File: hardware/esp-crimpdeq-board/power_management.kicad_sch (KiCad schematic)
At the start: 0 parts

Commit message: Added power management
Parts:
- added C15, C16: 4.7uF 16V, Capacitor_SMD:C_0603_1608Metric, symbol Device:C_Small
- added C22, C24: 0.1uF 10V, Capacitor_SMD:C_0402_1005Metric, symbol Device:C_Small
- added C23, C25: 1uF 16V, Capacitor_SMD:C_0402_1005Metric, symbol Device:C_Small
- added C28, C5, C7: 10uF 16V, Capacitor_SMD:C_0805_2012Metric, symbol Device:C_Small
- added C6: 22pF 50V, Capacitor_SMD:C_0603_1608Metric, symbol Device:C_Small
- added D3: LED, LED_SMD:LED_0603_1608Metric, symbol Device:LED
- added D4, D6: B5819W, Diode_SMD:D_SOD-123, symbol Device:D_Schottky
- added D5, D7, D8: LESD5D5.0CT1G, Diode_SMD:D_SOD-523, symbol Device:D_TVS
- added J1: USB4105-GF-A, PCM_GCT:GCT_USB4105-GF-A, symbol PCM_GCT:USB4105-GF-A
- added L1: SPH4018H2R2MT (2.2uH 2.2A), Inductor_SMD:L_Bourns-SRN4018, symbol Device:L_Small
- added Q1: DMG3415U, Package_TO_SOT_SMD:SOT-23, symbol Transistor_FET:DMG2301L
- added R1, R20, R23, R9: 10kR 1%, Resistor_SMD:R_0402_1005Metric, symbol Device:R_Small_US
- added R14: 1kR 1%, Resistor_SMD:R_0402_1005Metric, symbol Device:R_Small_US
- added R15, R2: 100kR 1%, Resistor_SMD:R_0402_1005Metric, symbol Device:R_Small_US
- added R3: 22k1R 1%, Resistor_SMD:R_0402_1005Metric, symbol Device:R_Small_US
- added R4, R6: 5k1R 1%, Resistor_SMD:R_0402_1005Metric, symbol Device:R_Small_US
- added R5: 0R 1%, Resistor_SMD:R_0402_1005Metric, symbol Device:R_Small_US
- added S1: 450404015514, PCM_Wurth_Elektronik:450404015514, symbol PCM_Wurth_Elektronik:450404015514
- added U3: REF35330QDBVR, Package_TO_SOT_SMD:SOT-23-6, symbol Reference_Voltage:REF35330QDBVR
- added U4: MCP1640Bx-xMC, Package_DFN_QFN:DFN-8-1EP_3x2mm_P0.5mm_EP1.75x1.45mm, symbol Regulator_Switching:MCP1640Bx-xMC
- added U6: MCP73831T-2ACI/OT, Package_TO_SOT_SMD:SOT-23-5, symbol Battery_Management:MCP73831-2-OT
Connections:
- new net: C6.2, R2.2, R3.1
- new net: R1.2, S1.3
- new net: J1.B5 (CC2), R4.1
- new net: J1.A5 (CC1), R6.1
- new net: D6.2 (A), D7.1 (A1), J1.A4_B9 (VBUS), J1.B4_A9 (VBUS)
- new net: R9.2, U6.5 (PROG)
- new net: D3.1 (K), R14.2
- new net: C28.1, U3.5 (NR)
- new net: U4.2 (GND), U4.3 (GND), U4.9 (GND)
- new net: U4.6 (V_{OUT}), U4.7 (V_{OUT})
- new net: R23.1, U3.3 (EN)
- new net: J1.S1 (SHELL_GND), J1.S2 (SHELL_GND), J1.S3 (SHELL_GND), J1.S4 (SHELL_GND), R5.1
- new net +3V3: C6.1, C7.1, L1.2, R2.1, R20.2, R23.2
- new net +5V: C22.1, C23.1, C5.1, D4.1 (K), Q1.2 (S), R1.1, U3.4 (VIN)
- new net +BATT_SYS: C16.1, Q1.3 (D), U6.3 (V_{BAT})
- new net Buck_Coil: L1.1
- new net CHARGING: R14.1, R20.1, U6.1 (STAT)
- new net ENABLE: S1.2
- new net GND: C15.1, C16.2, C22.2, C23.2, C24.2, C25.2, C28.2, C5.2, C7.2, D5.2 (A2), D7.2 (A2), D8.2 (A2), J1.A1_B12 (GND), J1.B1_A12 (GND), R15.2, R3.2, R4.2, R5.2, R6.2, R9.1, S1.1, U3.1 (GND), U3.2 (GND), U6.2 (V_{SS})
- new net USB_D+: D8.1 (A1), J1.A6 (DP1), J1.B6 (DP2)
- new net USB_D-: D5.1 (A1), J1.A7 (DN1), J1.B7 (DN2)
- new net VBUS: C15.2, D3.2 (A), D4.2 (A), D6.1 (K), Q1.1 (G), R15.1, U6.4 (V_{DD})
- new net VREF3V3: C24.1, C25.1, U3.6 (VREF)
- no-connect marks 0 -> 2
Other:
- note added: "DC/DC Buck Converter 3V3 Rails"
- note added: "Li-Ion Charge Management Controller"
- note added: "REF. VOLTAGE"
- note added: "Red LED 060 Charging"
- note added: "SIMPLE ON/OFF"
- note added: "USB & Battery Switch"
- note added: "USB Type-C Connector"

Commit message: Pending
Pending
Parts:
- removed U4: MCP1640Bx-xMC, Package_DFN_QFN:DFN-8-1EP_3x2mm_P0.5mm_EP1.75x1.45mm, symbol Regulator_Switching:MCP1640Bx-xMC
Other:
- moved on the sheet: C15, C16, C22, C23, C24, C25, C28, D3, D4, D5, D6, D7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

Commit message: Added secns SY8088 to produce 5 V for fast adc
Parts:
- added C32, C34: 10uF 16V, Capacitor_SMD:C_0805_2012Metric, symbol Device:C_Small
- added C33: 22pF 50V, Capacitor_SMD:C_0603_1608Metric, symbol Device:C_Small
- added L2: SPH4018H2R2MT (2.2uH 2.2A), Inductor_SMD:L_Bourns-SRN4018, symbol Device:L_Small
- added R10: 162kR 1%, Resistor_SMD:R_0402_1005Metric, symbol Device:R_Small_US
- added R13: 22k1R 1%, Resistor_SMD:R_0402_1005Metric, symbol Device:R_Small_US
- added U4, U5: SY8088, Package_TO_SOT_SMD:SOT-23-5, symbol PCM_Silergy:SY8088
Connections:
- net +5V: now also C33.1, C34.1, L2.2, R10.1; no longer C5.1, D4.1 (K), Q1.2 (S), R1.1
- net Buck_Coil: now also L2.1, U4.3 (LX), U5.3 (LX)
- net ENABLE: now also U4.1 (EN), U5.1 (EN)
- net GND: now also C32.2, C34.2, R13.2, U4.2 (GND), U5.2 (GND)
- net at C6.2, R2.2, R3.1: now also U4.5 (FB)
- new net: C33.2, R10.2, R13.1, U5.5 (FB)
- new net VSYS: C32.1, C5.1, D4.1 (K), Q1.2 (S), R1.1, U4.4 (IN), U5.4 (IN)
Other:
- note added: "DC/DC Buck Converter 5V0 Rails"
- moved on the sheet: C5, C6, C7, L1, R2, R3

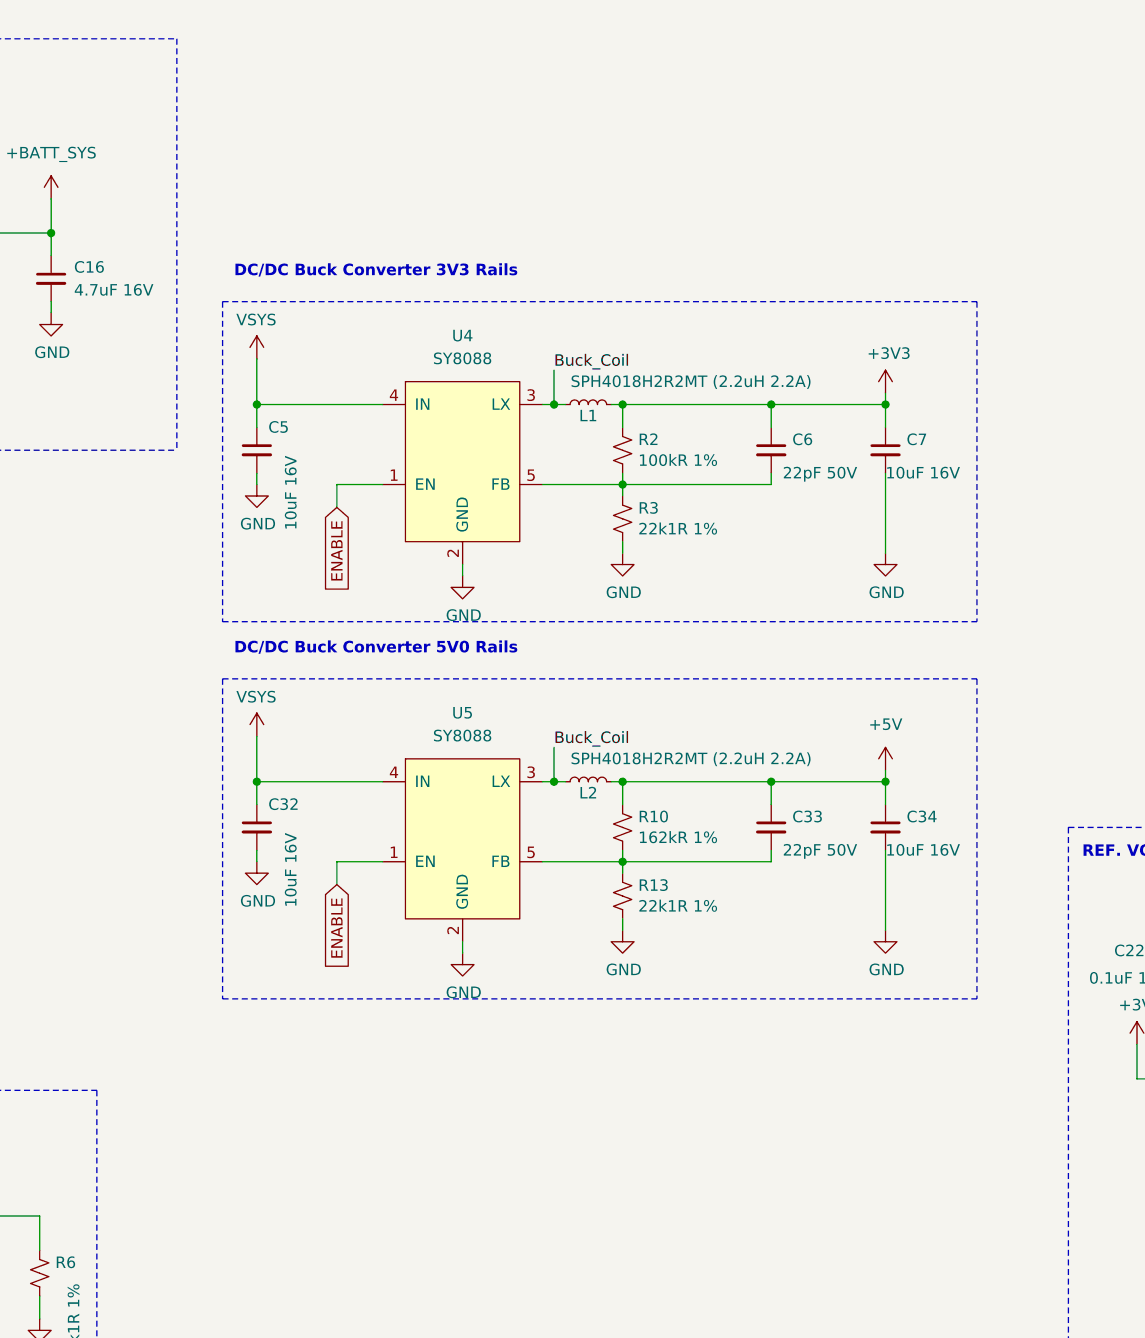
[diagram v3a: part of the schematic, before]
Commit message: Ordering sdchematic in different sheets
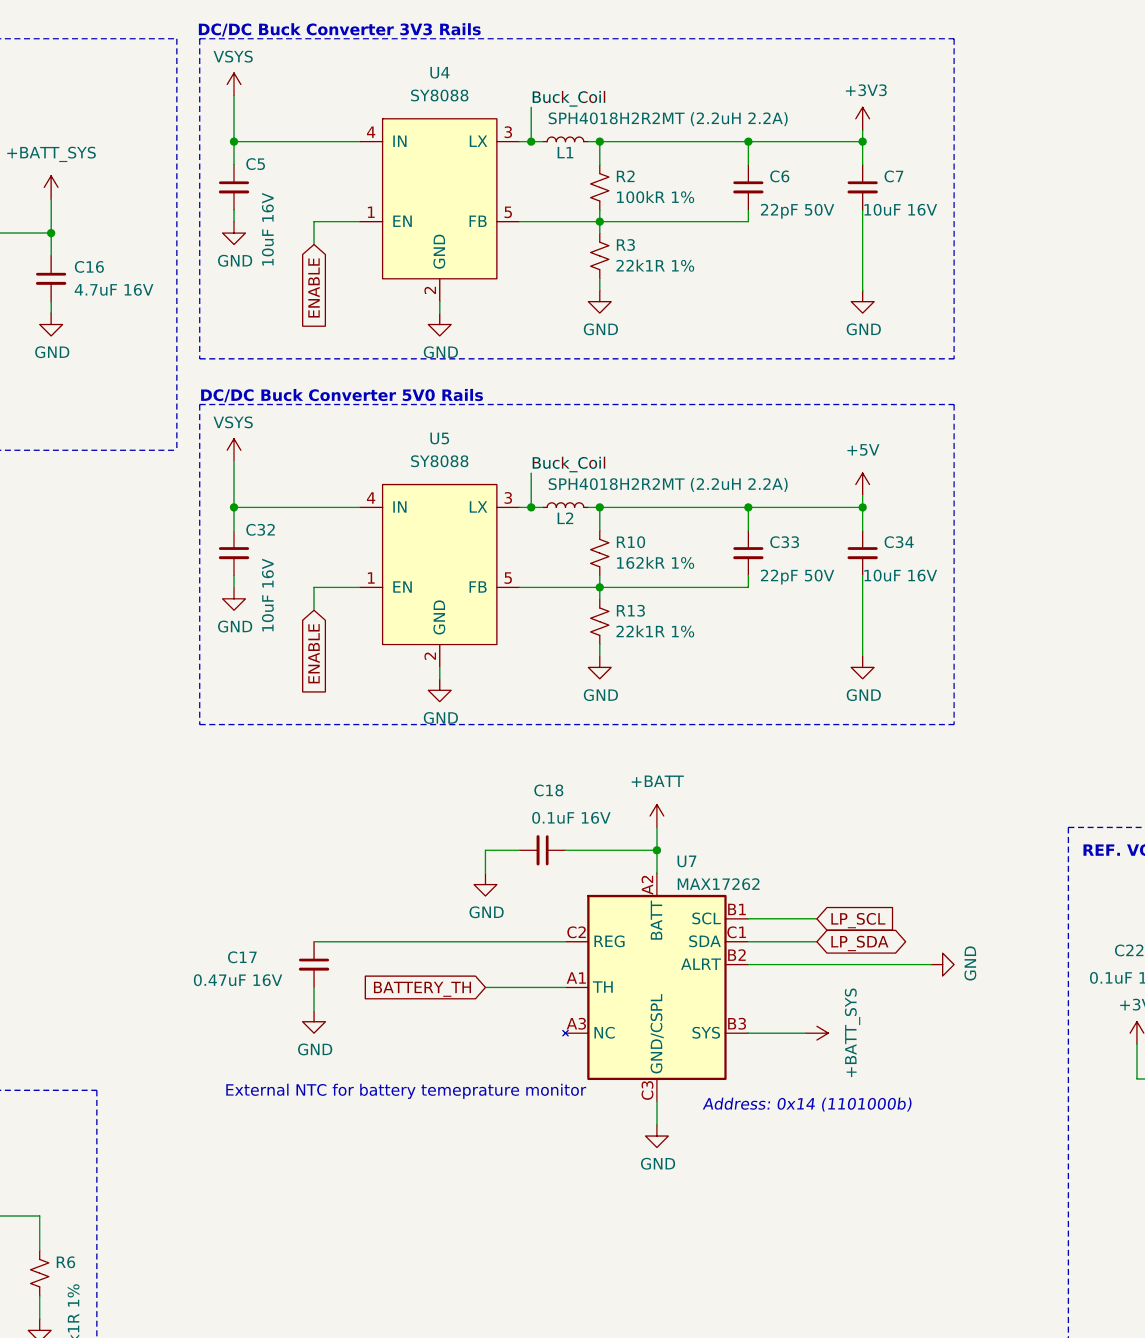
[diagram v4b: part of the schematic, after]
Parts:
- added C17: 0.47uF 16V, Capacitor_SMD:C_0603_1608Metric, symbol Device:C_Small
- added C18: 0.1uF 16V, Capacitor_SMD:C_0603_1608Metric, symbol Device:C_Small
- added U7: MAX17262, Package_BGA:WLP-9_1.468x1.448mm_Layout3x3_P0.4mm, symbol PCM_Maxim:MAX17262
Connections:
- net +BATT_SYS: now also U7.B3 (SYS)
- net GND: now also C17.2, C18.2, U7.B2 (ALRT), U7.C3 (GND/CSPL)
- new net: C17.1, U7.C2 (REG)
- new net +BATT: C18.1, U7.A2 (BATT)
- new net BATTERY_TH: U7.A1 (TH)
- new net LP_SCL: U7.B1 (SCL)
- new net LP_SDA: U7.C1 (SDA)
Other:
- note added: "Address: 0x14 (1101000b)"
- note added: "External NTC for battery temeprature monitor"
- moved on the sheet: C32, C33, C34, C5, C6, C7, L1, L2, R10, R13, R2, R3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

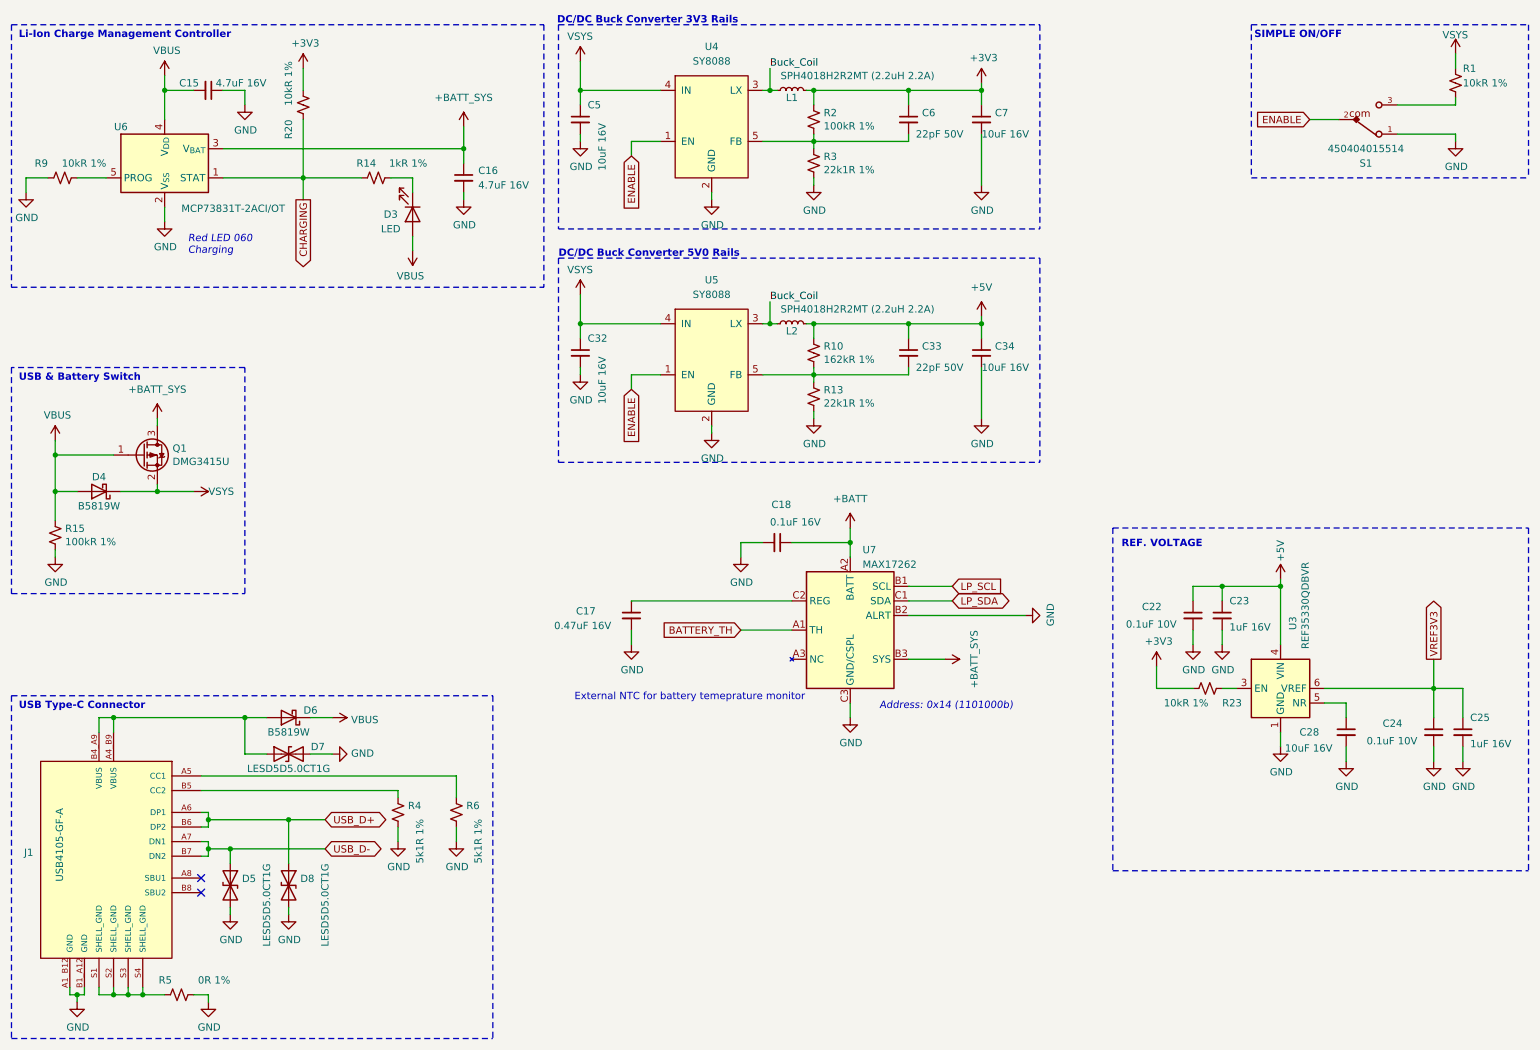
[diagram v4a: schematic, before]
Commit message: Cleaned schematic
- Pending connectors
- Pending BOM and footprints review
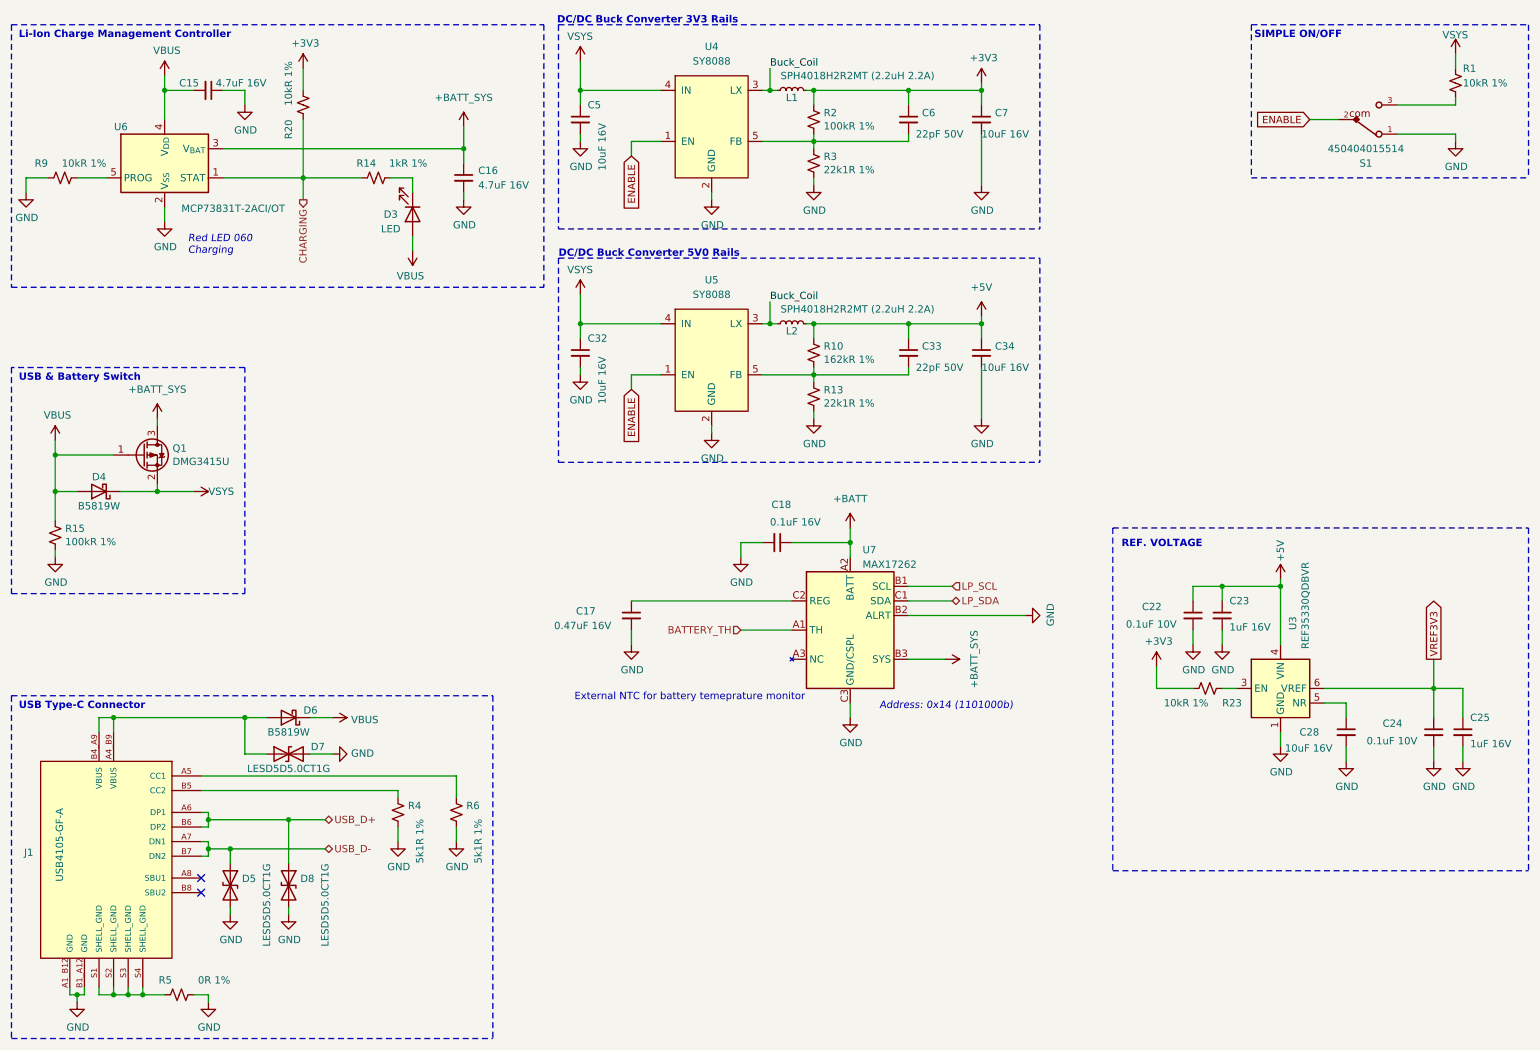
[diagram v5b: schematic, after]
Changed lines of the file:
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@@
-		)
-	)
-	(global_label "BATTERY_TH"
-		(shape input)
-		(at 143.51 120.65 180)
-		(fields_autoplaced yes)
-		(effects
-			(font
-				(size 1.27 1.27)
-			)
-			(justify right)
-		)
-		(property "Intersheetrefs" "${INTERSHEET_REFS}"
-			(at 130.1119 120.65 0)
-			(effects
-				(font
-					(size 1.27 1.27)
-				)
-				(justify right)
-				(hide yes)
-			)
-		)
-	)
-	(global_label "CHARGING"
-		(shape output)
-		(at 67.31 45.72 270)
-		(fields_autoplaced yes)
-		(effects
-			(font
-				(size 1.27 1.27)
-			)
-			(justify right)
-		)
-		(property "Intersheetrefs" "${INTERSHEET_REFS}"
-			(at 67.31 57.4854 90)
-			(effects
-				(font
-					(size 1.27 1.27)
-				)
-				(justify right)
-				(hide yes)
-			)
-		)
-	)
-	(global_label "USB_D+"
-		(shape bidirectional)
-		(at 71.12 153.67 0)
-		(fields_autoplaced yes)
-		(effects
-			(font
-				(size 1.27 1.27)
-			)
-			(justify left)
-		)
-		(property "Intersheetrefs" "${INTERSHEET_REFS}"
-			(at 82.0235 153.67 0)
-			(effects
-				(font
-					(size 1.27 1.27)
-				)
-				(justify left)
-				(hide yes)
-			)
-		)
-	)
-	(global_label "LP_SDA"
-		(shape bidirectional)
-		(at 180.34 115.57 0)
-		(fields_autoplaced yes)
-		(effects
-			(font
-				(size 1.27 1.27)
-			)
-			(justify left)
-		)
-		(property "Intersheetrefs" "${INTERSHEET_REFS}"
-			(at 190.4573 115.57 0)
-			(effects
-				(font
-					(size 1.27 1.27)
-				)
-				(justify left)
-				(hide yes)
-			)
 		)
 	)
@@
 		(property "Intersheetrefs" "${INTERSHEET_REFS}"
 			(at 264.16 115.2952 90)
-			(effects
-				(font
-					(size 1.27 1.27)
-				)
-				(justify left)
-				(hide yes)
-			)
-		)
-	)
-	(global_label "USB_D-"
-		(shape bidirectional)
-		(at 71.12 158.75 0)
-		(fields_autoplaced yes)
-		(effects
-			(font
-				(size 1.27 1.27)
-			)
-			(justify left)
-		)
-		(property "Intersheetrefs" "${INTERSHEET_REFS}"
-			(at 82.0235 158.75 0)
 			(effects
 				(font
@@
 				)
 				(justify right)
-				(hide yes)
-			)
-		)
-	)
-	(global_label "LP_SCL"
-		(shape input)
-		(at 180.34 113.03 0)
-		(fields_autoplaced yes)
-		(effects
-			(font
-				(size 1.27 1.27)
-			)
-			(justify left)
-		)
-		(property "Intersheetrefs" "${INTERSHEET_REFS}"
-			(at 189.4443 113.03 0)
-			(effects
-				(font
-					(size 1.27 1.27)
-				)
-				(justify left)
 				(hide yes)
 			)
@@
 		)
 	)
+	(hierarchical_label "LP_SDA"
+		(shape bidirectional)
+		(at 180.34 115.57 0)
+		(effects
+			(font
+				(size 1.27 1.27)
+			)
+			(justify left)
+		)
+	)
+	(hierarchical_label "CHARGING"
+		(shape output)
+		(at 67.31 45.72 270)
+		(effects
+			(font
+				(size 1.27 1.27)
+			)
+			(justify right)
+		)
+	)
+	(hierarchical_label "USB_D+"
+		(shape bidirectional)
+		(at 71.12 153.67 0)
+		(effects
+			(font
+				(size 1.27 1.27)
+			)
+			(justify left)
+		)
+	)
+	(hierarchical_label "USB_D-"
+		(shape bidirectional)
+		(at 71.12 158.75 0)
+		(effects
+			(font
+				(size 1.27 1.27)
+			)
+			(justify left)
+		)
+	)
+	(hierarchical_label "BATTERY_TH"
+		(shape input)
+		(at 143.51 120.65 180)
+		(effects
+			(font
+				(size 1.27 1.27)
+			)
+			(justify right)
+		)
+	)
+	(hierarchical_label "LP_SCL"
+		(shape input)
+		(at 180.34 113.03 0)
+		(effects
+			(font
+				(size 1.27 1.27)
+			)
+			(justify left)
+		)
+	)
